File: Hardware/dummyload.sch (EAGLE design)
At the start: 47 parts, among them IC1 MCP1700, Q1 IRFB7430PBF, SW1 SWITCH-B3U-1110-BOSS, U1 ATMEGA32U4-AU, U2 LMP2022, U3 MCP3426, U4 MAX5812, X1 USB-MINI/MICRO-4S-4LEGS, Y1 16MHz

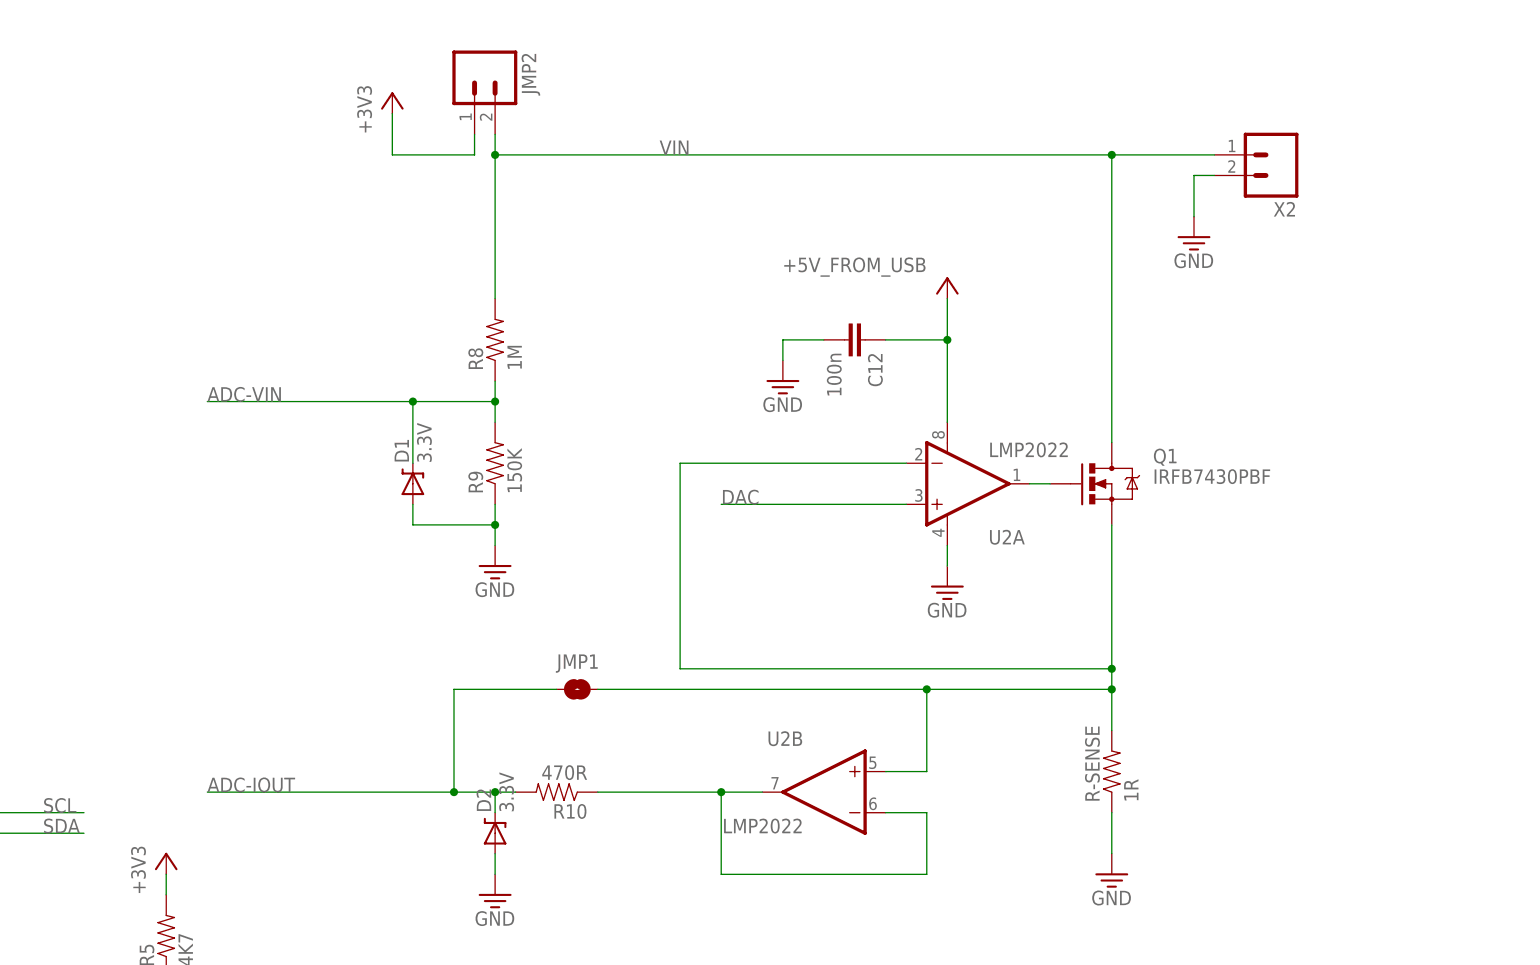
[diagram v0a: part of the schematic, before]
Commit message: updated to use 0.5 ohm cur sense resistor
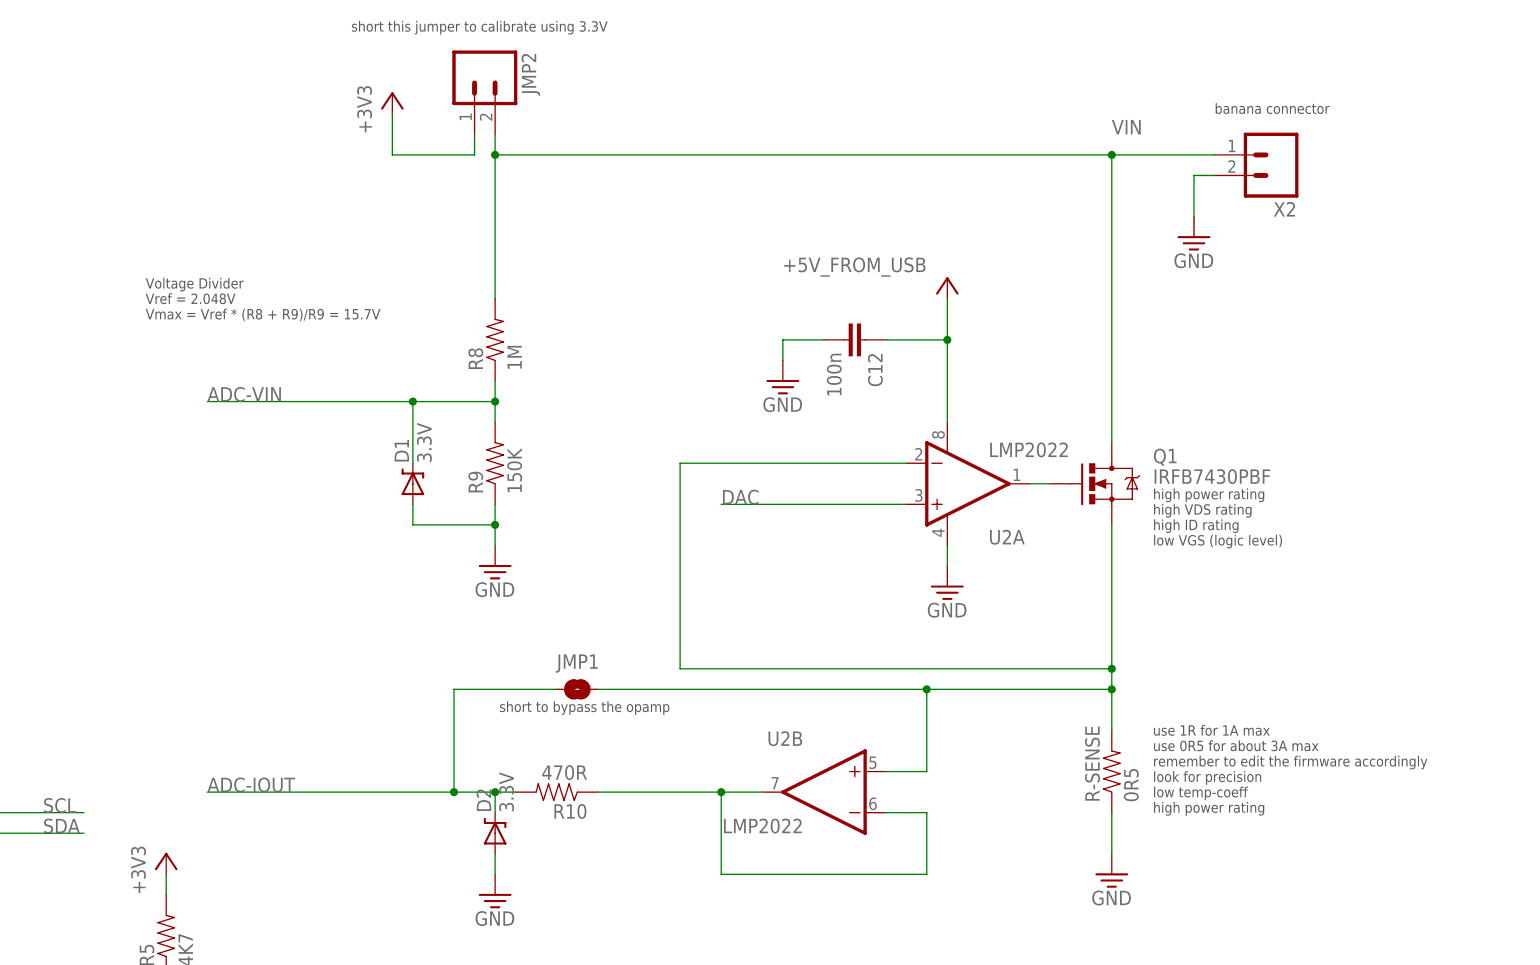
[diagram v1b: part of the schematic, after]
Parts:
- R-SENSE: value 1R -> 0R5
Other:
- note added: "Voltage Divider Vref = 2.048V Vmax = Vref * (R8 + R9)/R9 = 15.7V"
- note added: "banana connector"
- note added: "high power rating high VDS rating high ID rating low VGS (logic level)"
- note added: "short this jumper to calibrate using 3.3V"
- note added: "short to bypass the opamp"
- note added: "use 1R for 1A max use 0R5 for about 3A max remember to edit the firmware accordingly look for precision low temp-coeff high power rating"
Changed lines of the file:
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@@
 <grid distance="0.1" unitdist="inch" unit="inch" style="lines" multiple="1" display="no" altdistance="0.01" altunitdist="inch" altunit="inch"/>
 <layers>
-<layer number="1" name="Top" color="4" fill="1" visible="no" active="no"/>
-<layer number="2" name="Route2" color="1" fill="3" visible="no" active="no"/>
-<layer number="3" name="Route3" color="4" fill="3" visible="no" active="no"/>
-<layer number="4" name="Route4" color="1" fill="4" visible="no" active="no"/>
-<layer number="5" name="Route5" color="4" fill="4" visible="no" active="no"/>
-<layer number="6" name="Route6" color="1" fill="8" visible="no" active="no"/>
-<layer number="7" name="Route7" color="4" fill="8" visible="no" active="no"/>
-<layer number="8" name="Route8" color="1" fill="2" visible="no" active="no"/>
-<layer number="9" name="Route9" color="4" fill="2" visible="no" active="no"/>
-<layer number="10" name="Route10" color="1" fill="7" visible="no" active="no"/>
-<layer number="11" name="Route11" color="4" fill="7" visible="no" active="no"/>
-<layer number="12" name="Route12" color="1" fill="5" visible="no" active="no"/>
-<layer number="13" name="Route13" color="4" fill="5" visible="no" active="no"/>
-<layer number="14" name="Route14" color="1" fill="6" visible="no" active="no"/>
-<layer number="15" name="Route15" color="4" fill="6" visible="no" active="no"/>
-<layer number="16" name="Bottom" color="1" fill="1" visible="no" active="no"/>
-<layer number="17" name="Pads" color="2" fill="1" visible="no" active="no"/>
-<layer number="18" name="Vias" color="14" fill="1" visible="no" active="no"/>
-<layer number="19" name="Unrouted" color="6" fill="1" visible="no" active="no"/>
-<layer number="20" name="Dimension" color="15" fill="1" visible="no" active="no"/>
-<layer number="21" name="tPlace" color="7" fill="1" visible="no" active="no"/>
-<layer number="22" name="bPlace" color="7" fill="1" visible="no" active="no"/>
-<layer number="23" name="tOrigins" color="15" fill="1" visible="no" active="no"/>
-<layer number="24" name="bOrigins" color="15" fill="1" visible="no" active="no"/>
-<layer number="25" name="tNames" color="7" fill="1" visible="no" active="no"/>
-<layer number="26" name="bNames" color="7" fill="1" visible="no" active="no"/>
-<layer number="27" name="tValues" color="7" fill="1" visible="no" active="no"/>
-<layer number="28" name="bValues" color="7" fill="1" visible="no" active="no"/>
+<layer number="1" name="Top" color="4" fill="1" visible="yes" active="no"/>
+<layer number="2" name="Route2" color="1" fill="3" visible="yes" active="no"/>
+<layer number="3" name="Route3" color="4" fill="3" visible="yes" active="no"/>
+<layer number="4" name="Route4" color="1" fill="4" visible="yes" active="no"/>
+<layer number="5" name="Route5" color="4" fill="4" visible="yes" active="no"/>
+<layer number="6" name="Route6" color="1" fill="8" visible="yes" active="no"/>
+<layer number="7" name="Route7" color="4" fill="8" visible="yes" active="no"/>
+<layer number="8" name="Route8" color="1" fill="2" visible="yes" active="no"/>
+<layer number="9" name="Route9" color="4" fill="2" visible="yes" active="no"/>
+<layer number="10" name="Route10" color="1" fill="7" visible="yes" active="no"/>
+<layer number="11" name="Route11" color="4" fill="7" visible="yes" active="no"/>
+<layer number="12" name="Route12" color="1" fill="5" visible="yes" active="no"/>
+<layer number="13" name="Route13" color="4" fill="5" visible="yes" active="no"/>
+<layer number="14" name="Route14" color="1" fill="6" visible="yes" active="no"/>
+<layer number="15" name="Route15" color="4" fill="6" visible="yes" active="no"/>
+<layer number="16" name="Bottom" color="1" fill="1" visible="yes" active="no"/>
+<layer number="17" name="Pads" color="2" fill="1" visible="yes" active="no"/>
+<layer number="18" name="Vias" color="14" fill="1" visible="yes" active="no"/>
+<layer number="19" name="Unrouted" color="6" fill="1" visible="yes" active="no"/>
+<layer number="20" name="Dimension" color="15" fill="1" visible="yes" active="no"/>
+<layer number="21" name="tPlace" color="7" fill="1" visible="yes" active="no"/>
+<layer number="22" name="bPlace" color="7" fill="1" visible="yes" active="no"/>
+<layer number="23" name="tOrigins" color="15" fill="1" visible="yes" active="no"/>
+<layer number="24" name="bOrigins" color="15" fill="1" visible="yes" active="no"/>
+<layer number="25" name="tNames" color="7" fill="1" visible="yes" active="no"/>
+<layer number="26" name="bNames" color="7" fill="1" visible="yes" active="no"/>
+<layer number="27" name="tValues" color="7" fill="1" visible="yes" active="no"/>
+<layer number="28" name="bValues" color="7" fill="1" visible="yes" active="no"/>
 <layer number="29" name="tStop" color="7" fill="3" visible="no" active="no"/>
 <layer number="30" name="bStop" color="7" fill="6" visible="no" active="no"/>
@@
 <layer number="35" name="tGlue" color="7" fill="4" visible="no" active="no"/>
 <layer number="36" name="bGlue" color="7" fill="5" visible="no" active="no"/>
-<layer number="37" name="tTest" color="7" fill="1" visible="no" active="no"/>
-<layer number="38" name="bTest" color="7" fill="1" visible="no" active="no"/>
+<layer number="37" name="tTest" color="7" fill="1" visible="yes" active="no"/>
+<layer number="38" name="bTest" color="7" fill="1" visible="yes" active="no"/>
 <layer number="39" name="tKeepout" color="4" fill="11" visible="no" active="no"/>
 <layer number="40" name="bKeepout" color="1" fill="11" visible="no" active="no"/>
@@
 <layer number="44" name="Drills" color="7" fill="1" visible="no" active="no"/>
 <layer number="45" name="Holes" color="7" fill="1" visible="no" active="no"/>
-<layer number="46" name="Milling" color="3" fill="1" visible="no" active="no"/>
-<layer number="47" name="Measures" color="7" fill="1" visible="no" active="no"/>
-<layer number="48" name="Document" color="7" fill="1" visible="no" active="no"/>
-<layer number="49" name="Reference" color="7" fill="1" visible="no" active="no"/>
-<layer number="50" name="dxf" color="7" fill="1" visible="no" active="no"/>
-<layer number="51" name="tDocu" color="7" fill="1" visible="no" active="no"/>
-<layer number="52" name="bDocu" color="7" fill="1" visible="no" active="no"/>
-<layer number="53" name="tGND_GNDA" color="7" fill="9" visible="no" active="no"/>
-<layer number="54" name="bGND_GNDA" color="1" fill="9" visible="no" active="no"/>
-<layer number="56" name="wert" color="7" fill="1" visible="no" active="no"/>
+<layer number="46" name="Milling" color="3" fill="1" visible="yes" active="no"/>
+<layer number="47" name="Measures" color="7" fill="1" visible="yes" active="no"/>
+<layer number="48" name="Document" color="7" fill="1" visible="yes" active="no"/>
+<layer number="49" name="Reference" color="7" fill="1" visible="yes" active="no"/>
+<layer number="50" name="dxf" color="7" fill="1" visible="yes" active="no"/>
+<layer number="51" name="tDocu" color="7" fill="1" visible="yes" active="no"/>
+<layer number="52" name="bDocu" color="7" fill="1" visible="yes" active="no"/>
+<layer number="53" name="tGND_GNDA" color="7" fill="9" visible="yes" active="no"/>
+<layer number="54" name="bGND_GNDA" color="1" fill="9" visible="yes" active="no"/>
+<layer number="56" name="wert" color="7" fill="1" visible="yes" active="no"/>
 <layer number="91" name="Nets" color="2" fill="1" visible="yes" active="yes"/>
 <layer number="92" name="Busses" color="1" fill="1" visible="yes" active="yes"/>
@@
 <part name="GND15" library="minilab" deviceset="GND" device=""/>
 <part name="Q1" library="minilab" deviceset="MOSFET-NCHANNEL" device="PTH2" value="IRFB7430PBF"/>
-<part name="R-SENSE" library="minilab" deviceset="RESISTOR" device="-D2PAK" value="1R"/>
+<part name="R-SENSE" library="minilab" deviceset="RESISTOR" device="-D2PAK" value="0R5"/>
 <part name="GND17" library="minilab" deviceset="GND" device=""/>
 <part name="U2" library="minilab" deviceset="LMP20X2" device="-MSOP8" value="LMP2022"/>
@@
 by Frank Zhao
 20130612</text>
+<text x="185.42" y="134.62" size="1.27" layer="97">Voltage Divider
+Vref = 2.048V
+Vmax = Vref * (R8 + R9)/R9 = 15.7V</text>
+<text x="210.82" y="170.18" size="1.27" layer="97">short this jumper to calibrate using 3.3V</text>
+<text x="317.5" y="160.02" size="1.27" layer="97">banana connector</text>
+<text x="309.88" y="73.66" size="1.27" layer="97">use 1R for 1A max
+use 0R5 for about 3A max
+remember to edit the firmware accordingly
+look for precision
+low temp-coeff
+high power rating</text>
+<text x="229.108" y="86.106" size="1.27" layer="97">short to bypass the opamp</text>
+<text x="309.88" y="106.68" size="1.27" layer="97">high power rating
+high VDS rating
+high ID rating
+low VGS (logic level)</text>
 </plain>
 <instances>
@@
 <wire x1="228.6" y1="137.16" x2="228.6" y2="154.94" width="0.1524" layer="91"/>
 <wire x1="228.6" y1="154.94" x2="304.8" y2="154.94" width="0.1524" layer="91"/>
-<label x="248.92" y="154.94" size="1.778" layer="95"/>
+<label x="304.8" y="157.48" size="1.778" layer="95"/>
 <pinref part="Q1" gate="G$1" pin="D"/>
 <wire x1="304.8" y1="154.94" x2="304.8" y2="119.38" width="0.1524" layer="91"/>
